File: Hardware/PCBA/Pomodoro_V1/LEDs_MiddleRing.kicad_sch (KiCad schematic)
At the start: 0 parts

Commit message: Updated CubeMx File, Created Schematic for µC, layouted the LEDs on the PCB
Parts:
- added C10, C12: 100n, symbol Device:C
- added C11, C9: 4u7, symbol Device:C
- added D61, D62, D63, D64, D65, D66, D67, D68, D69, D70, D71, D72, D73, D74, D75, D76, D77, D78, D79, D80, D81, D82, D83, D84, D85, D86, D87, D88, D89, D90: WS2812B-2020, LED_SMD:LED_WS2812B-2020_PLCC4_2.0x2.0mm, symbol LED:WS2812B-2020
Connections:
- new net: D66.1 (DOUT), D68.3 (DIN)
- new net: D64.1 (DOUT), D66.3 (DIN)
- new net: D80.1 (DOUT), D82.3 (DIN)
- new net: D78.1 (DOUT), D80.3 (DIN)
- new net: D63.1 (DOUT), D65.3 (DIN)
- new net: D61.1 (DOUT), D63.3 (DIN)
- new net: D70.1 (DOUT), D72.3 (DIN)
- new net: D68.1 (DOUT), D70.3 (DIN)
- new net: D81.1 (DOUT), D83.3 (DIN)
- new net: D79.1 (DOUT), D81.3 (DIN)
- new net: D88.1 (DOUT), D90.3 (DIN)
- new net: D85.1 (DOUT), D87.3 (DIN)
- new net: D83.1 (DOUT), D85.3 (DIN)
- new net: D62.1 (DOUT), D64.3 (DIN)
- new net: D62.3 (DIN), D89.1 (DOUT)
- new net: D87.1 (DOUT), D89.3 (DIN)
- new net: D86.1 (DOUT), D88.3 (DIN)
- new net: D73.1 (DOUT), D75.3 (DIN)
- new net: D71.1 (DOUT), D73.3 (DIN)
- new net: D84.1 (DOUT), D86.3 (DIN)
- new net: D76.1 (DOUT), D78.3 (DIN)
- new net: D74.1 (DOUT), D76.3 (DIN)
- new net: D77.1 (DOUT), D79.3 (DIN)
- new net: D75.1 (DOUT), D77.3 (DIN)
- new net: D69.1 (DOUT), D71.3 (DIN)
- new net: D72.1 (DOUT), D74.3 (DIN)
- new net: D65.1 (DOUT), D67.3 (DIN)
- new net: D67.1 (DOUT), D69.3 (DIN)
- new net: D82.1 (DOUT), D84.3 (DIN)
- new net +5V: C10.1, C11.1, C12.1, C9.1, D61.4 (VDD), D62.4 (VDD), D63.4 (VDD), D64.4 (VDD), D65.4 (VDD), D66.4 (VDD), D67.4 (VDD), D68.4 (VDD), D69.4 (VDD), D70.4 (VDD), D71.4 (VDD), D72.4 (VDD), D73.4 (VDD), D74.4 (VDD), D75.4 (VDD), D76.4 (VDD), D77.4 (VDD), D78.4 (VDD), D79.4 (VDD), D80.4 (VDD), D81.4 (VDD), D82.4 (VDD), D83.4 (VDD), D84.4 (VDD), D85.4 (VDD), D86.4 (VDD), D87.4 (VDD), D88.4 (VDD), D89.4 (VDD), D90.4 (VDD)
- new net GND: C10.2, C11.2, C12.2, C9.2, D61.2 (VSS), D62.2 (VSS), D63.2 (VSS), D64.2 (VSS), D65.2 (VSS), D66.2 (VSS), D67.2 (VSS), D68.2 (VSS), D69.2 (VSS), D70.2 (VSS), D71.2 (VSS), D72.2 (VSS), D73.2 (VSS), D74.2 (VSS), D75.2 (VSS), D76.2 (VSS), D77.2 (VSS), D78.2 (VSS), D79.2 (VSS), D80.2 (VSS), D81.2 (VSS), D82.2 (VSS), D83.2 (VSS), D84.2 (VSS), D85.2 (VSS), D86.2 (VSS), D87.2 (VSS), D88.2 (VSS), D89.2 (VSS), D90.2 (VSS)
- new net TIM1_CH1 (RgbLed Inner Ring): D90.1 (DOUT)
- new net TIM1_CH1 (RgbLed Middle Ring): D61.3 (DIN)

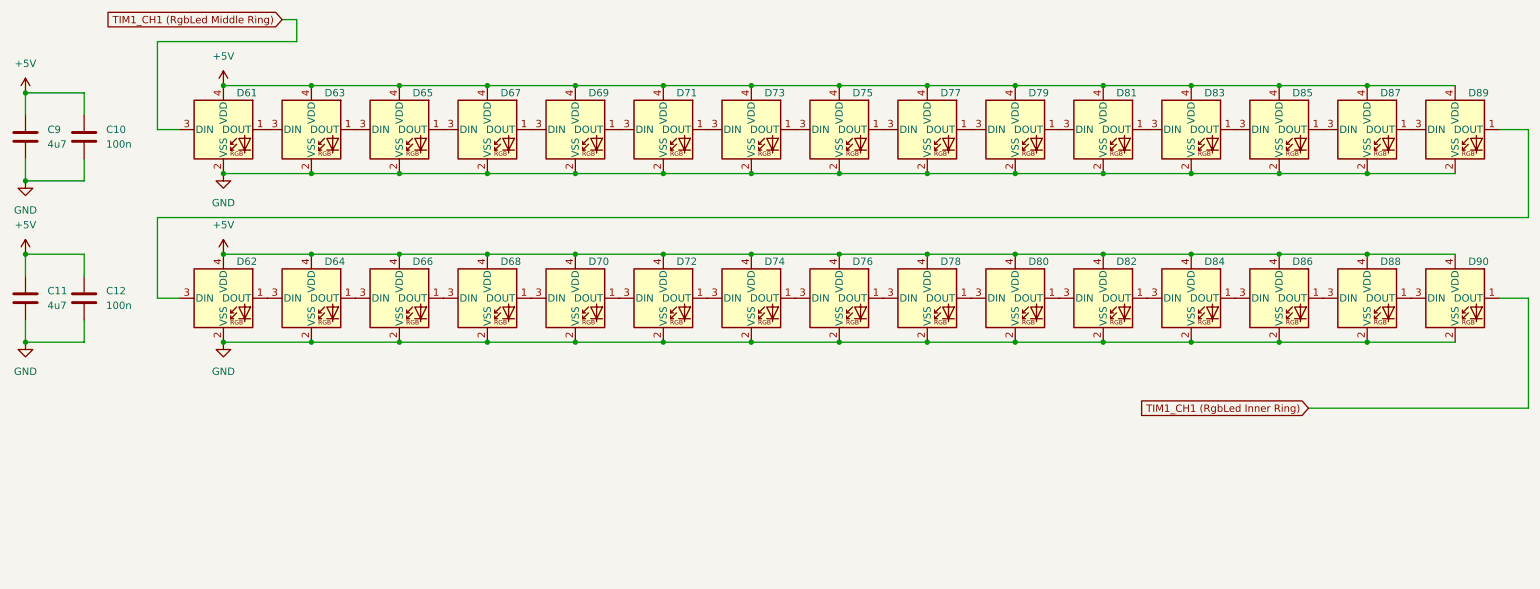
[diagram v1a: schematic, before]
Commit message: added the accelerometer to the Schematic
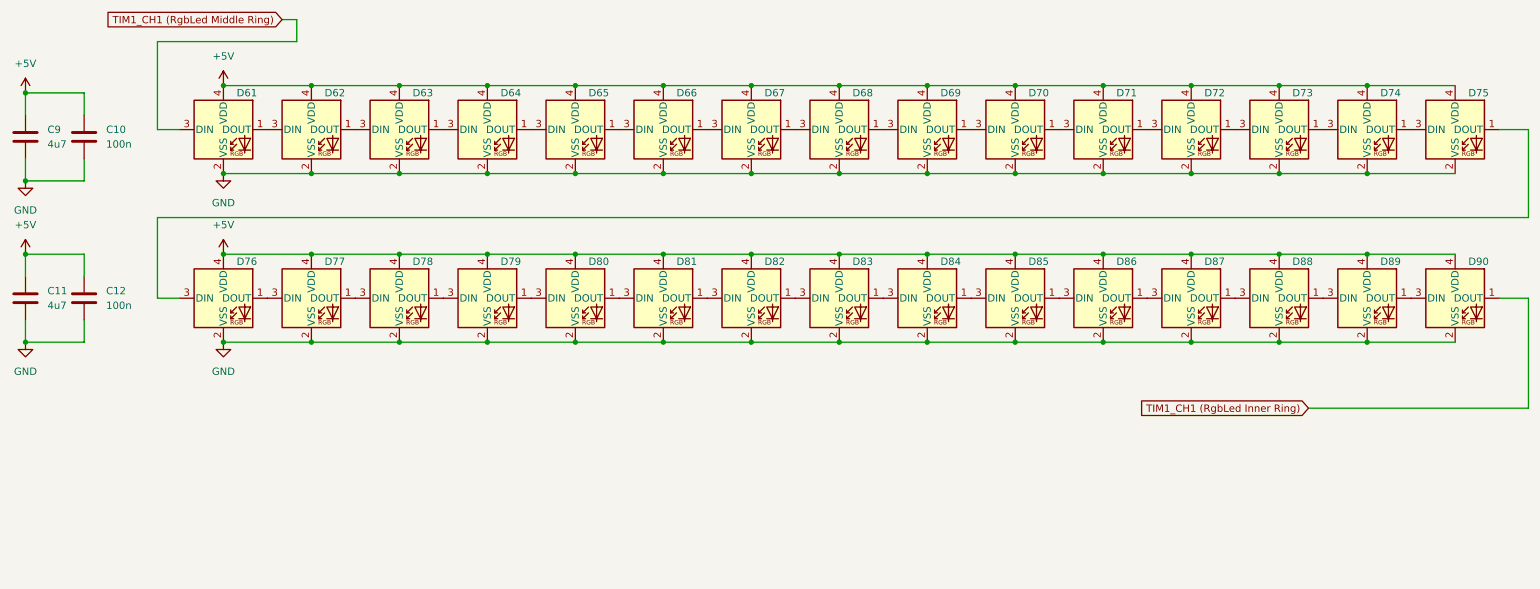
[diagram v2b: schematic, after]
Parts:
- renumbered D63 to D62, D65 to D63, D67 to D64, D69 to D65, D71 to D66, D73 to D67, D75 to D68, D77 to D69, D79 to D70, D81 to D71, D83 to D72, D85 to D73, D87 to D74, D89 to D75, D62 to D76, D64 to D77, D66 to D78, D68 to D79, D70 to D80, D72 to D81, D74 to D82, D76 to D83, D78 to D84, D80 to D85, D82 to D86, D84 to D87, D86 to D88, D88 to D89

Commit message: Implemented the Rotary encoder, the buttons, the IMU, Added it to the PCB (All the space constraining elements are now placed)
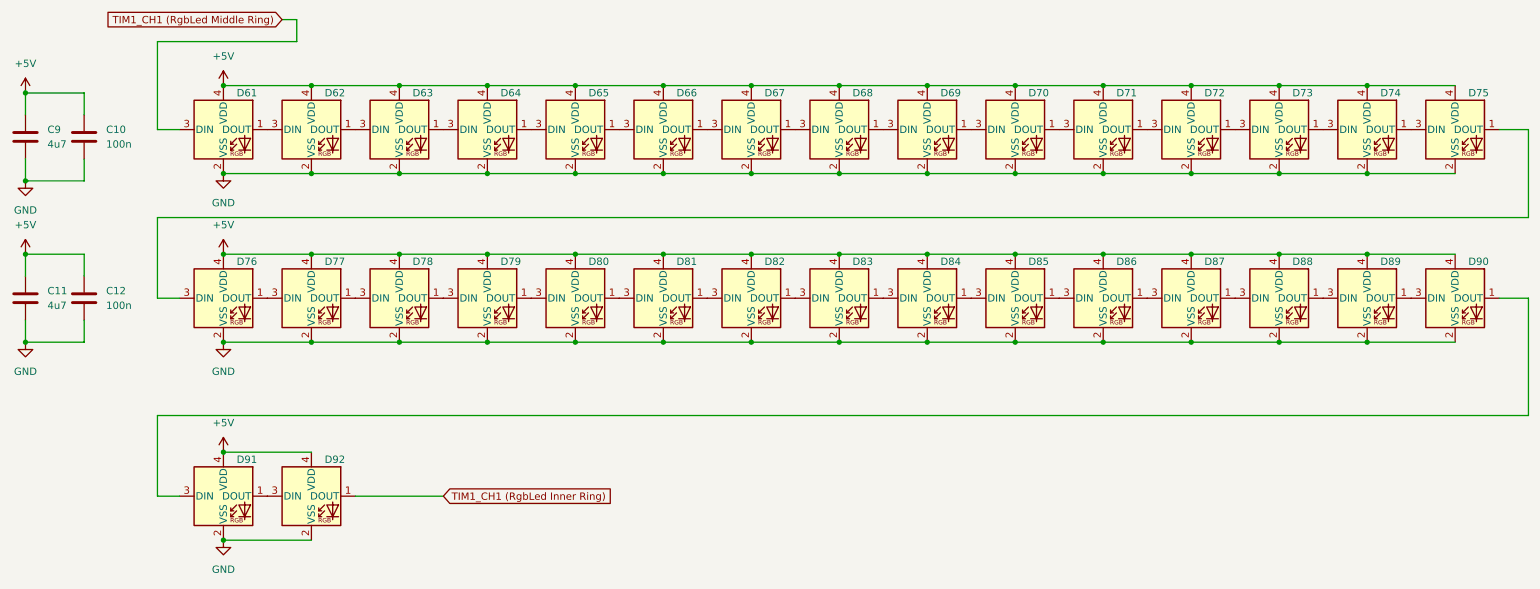
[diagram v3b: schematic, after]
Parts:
- added D91, D92: WS2812B-2020, LED_SMD:LED_WS2812B-2020_PLCC4_2.0x2.0mm, symbol LED:WS2812B-2020
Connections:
- net +5V: now also D91.4 (VDD), D92.4 (VDD)
- net GND: now also D91.2 (VSS), D92.2 (VSS)
- net TIM1_CH1 (RgbLed Inner Ring): now also D92.1 (DOUT); no longer D90.1 (DOUT)
- new net: D91.1 (DOUT), D92.3 (DIN)
- new net: D90.1 (DOUT), D91.3 (DIN)

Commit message: Finalized the schematic, First Draft of the finished Layout
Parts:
- removed C10, C12: 100n, symbol Device:C
- removed C11, C9: 4u7, symbol Device:C

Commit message: Version that was ordered online
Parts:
- D61, D62, D63, D64, D65, D66, D67, D68, D69, D70, D71, D72, D73, D74, D75, D76, D77, D78, D79, D80, D81, D82, D83, D84, D85, D86, D87, D88, D89, D90, D91, D92: MPN (none) -> WS2812B-2020
